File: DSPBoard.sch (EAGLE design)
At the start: 144 parts, among them IC1 AD1939WBSTZ, IC10 LM833N, IC11 LM833N, IC12 TL074P, IC2 25AA1024-I_SM, IC4 LM833N, IC5 LM833N, IC6 LM833N, IC7 LM833N, IC8 LM833N, IC9 LM833N, SW1 EC12E_SW, SW2 EC12E_SW, X1 2510-, Y1 12.288MHz

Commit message: futher effort and set 3v3 analog
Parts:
- removed C32, C33, C34, C35, C36, C37, C38, C39: 1u, rcl:C-EUC0805
- removed IC10, IC11, IC4, IC5, IC6, IC7, IC8, IC9: LM833N, linear:LM833N
- removed IC12: TL074P, linear:TL074P
- removed R30, R33, R37, R39: 200k, rcl:R-EU_R0603
- removed R31, R34, R38, R41: 33k, rcl:R-EU_R0603
- removed R32, R35, R36, R40: 100k, rcl:R-EU_R0603
- removed R42, R43, R44, R45, R46, R47, R48, R49, R50, R51: 10k, rcl:R-EU_R0603
- removed SW1, SW2: EC12E_SW, switch-alps:EC12E_SW
- removed U$13, U$14, U$15, U$16, U$17, U$18, U$19, U$20, U$21, U$22, U$23, U$24, U$5, U$6, U$7, U$9: WQP-PJ301M-12_JACK, thonkiconn:WQP-PJ301M-12_JACK
- removed VR1, VR2, VR7, VR8: 10k, SparkFun-Resistors:POTENTIOMETER-PTH-9MM-1/20W-20%-KIT
- added C45: (no value), rcl:C-EUC0805
- added IC3: LM4040B10DBZ, texas:LM4041B12DBZ
- added R16: (no value), rcl:R-EU_R0805
- added U$12, U$8: EEE-FK1C100R, LM11173p3:EEE-FK1C100R
- added U1: Value, LM11173p3:LM1117DTX-3.3/NOPB
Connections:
- removed net N$10: C32.1, IC12A.-IN, R30.2, R31.1, R32.1
- removed net N$11: R36.2, U$7.2
- removed net N$12: R30.1, VR1.S
- removed net N$13: R35.2, U$6.2
- removed net N$14: R33.2, VR2.S
- removed net N$15: C33.1, IC12B.-IN, R33.1, R34.1, R35.1
- removed net N$16: R37.2, VR7.S
- removed net N$17: C34.2, IC12C.-IN, R36.1, R37.1, R38.2
- removed net N$18: R39.2, VR8.S
- removed net N$19: R40.2, U$9.2
- removed net N$20: C35.2, IC12D.-IN, R39.1, R40.1, R41.2
- removed net N$22: R42.1, R45.1, SW1G$1.A
- removed net N$23: R43.2, R44.1, SW1G$1.B
- removed net N$25: R46.1, R49.1, SW2G$1.A
- removed net N$26: R47.2, R48.1, SW2G$1.B
- removed net N$9: R32.2, U$5.2
- removed net VSS: IC12A.+IN, IC12B.+IN, IC12C.+IN, IC12D.+IN
- new net 3V3A: U$8.+, U1.OUT
- net +3V3: no longer R44.2, R45.2, R48.2, R49.2, R50.1, R51.1
- net +5V: now also U$12.+, U1.INPUT
- net -10V: now also C45.1, IC3.A, R16.1; no longer VR1.A, VR2.A, VR7.A, VR8.A
- net -12V: now also R16.2
- net CV0: no longer C32.2, IC12A.OUT, R31.2
- net CV1: no longer C33.2, IC12B.OUT, R34.2
- net CV2: no longer C34.1, IC12C.OUT, R38.1
- net CV3: no longer C35.1, IC12D.OUT, R41.1
- net ENCODER0_0: no longer C36.1, R42.2
- net ENCODER0_1: no longer C37.1, R43.1
- net ENCODER0_2: no longer R50.2, SW1G$2.1
- net ENCODER1_0: no longer C38.1, R46.2
- net ENCODER1_1: no longer C39.1, R47.1
- net ENCODER1_2: no longer R51.2, SW2G$2.1
- net GND: now also C45.2, IC3.C, U$12.-, U$8.-, U1.GND; no longer C36.2, C37.2, C38.2, C39.2, SW1G$1.C, SW1G$2.2, SW2G$1.C, SW2G$2.2, U$5.1, U$5.3, U$6.1, U$6.3, U$7.1, U$7.3, U$9.1, U$9.3, VR1.E, VR2.E, VR7.E, VR8.E
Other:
- note added: "3v3 Analog Supply"
- note added: "3v3 Digital Supply"
- note removed: "3v2 Digital Supply"
- note removed: "Rotary Encoders"
- note removed: "This circuit is Biased by VSS at ~1v2 to give a 0 <> 3v3 signal"

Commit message: added input single to differential circuit
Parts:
- added C32: 22u, rcl:C-EUC0805
- added C33, C34, C35, C36, C37, C38, C39, C46, C47, C48, C49, C50, C51, C52, C53, C54, C55, C56, C57, C58, C59, C60, C61, C62, C63, C64, C65, C66, C67, C68, C69, C70, C71, C72, C73, C74, C75, C76, C77, C78: (no value), rcl:C-EUC0805
- added IC4, IC5, IC6, IC7: LM833D, linear:LM833D
- added R30: 480, rcl:R-EU_R0805
- added R31, R33, R34, R35, R36, R37, R38, R39, R40, R41, R42, R43, R44, R45, R46, R47, R48, R49, R50, R51, R55, R57, R61, R62, R63, R64, R65, R66, R67, R68, R69, R70, R71, R72, R73, R74, R75, R76, R77, R78: (no value), rcl:R-EU_R0805
- added R32: 10k, rcl:R-EU_R0805
- added U$21, U$5, U$6, U$7: WQP-PJ301M-12_JACK, thonkiconn:WQP-PJ301M-12_JACK
- added VR1: (no value), v-reg:TL431CLP
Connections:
- new net 1VREF: C32.1, R30.2, R32.2, VR1.C, VR1.R
- new net AIN0+: C47.1, C48.1, IC1.ADC1LP, R40.1
- new net AIN0-: C46.2, C47.2, IC1.ADC1LN, R41.1
- new net AIN1+: C57.1, C58.1, IC1.ADC1RP, R50.1
- new net AIN1-: C56.2, C57.2, IC1.ADC1RN, R51.1
- new net AIN2+: C67.1, C68.1, IC1.ADC2LP, R67.1
- new net AIN2-: C66.2, C67.2, IC1.ADC2LN, R68.1
- new net AIN3+: C76.2, C77.2, IC1.ADC2RP, R78.1
- new net AIN3-: C77.1, C78.1, IC1.ADC2RN, R77.1
- new net N$10: C35.2, R31.1
- new net N$11: C36.1, R31.2, R33.1, R39.2
- new net N$12: C37.2, IC4A.+IN, R33.2
- new net N$13: IC4B.-IN, R34.1, R35.2
- new net N$14: C36.2, IC4A.-IN, IC4A.OUT, R34.2, R41.2
- new net N$15: IC4B.OUT, R35.1, R40.2
- new net N$16: C38.2, IC4B.+IN, R36.1
- new net N$18: C38.1, C39.1, R36.2, R37.2, R38.1, R39.1
- new net N$19: C39.2, R37.1
- new net N$20: C46.1, C48.2
- new net N$23: C51.1, U$5.2
- new net N$25: C51.2, R42.1
- new net N$26: C52.1, R42.2, R43.1, R49.2
- new net N$34: C53.2, IC5A.+IN, R43.2
- new net N$36: C52.2, IC5A.-IN, IC5A.OUT, R44.2, R51.2
- new net N$38: IC5B.-IN, R44.1, R45.2
- new net N$42: IC5B.OUT, R45.1, R50.2
- new net N$43: C54.2, IC5B.+IN, R46.1
- new net N$44: C54.1, C55.1, R46.2, R47.2, R48.1, R49.1
- new net N$45: C55.2, R47.1
- new net N$46: C56.1, C58.2
- new net N$47: C61.1, U$6.2
- new net N$48: C61.2, R55.1
- new net N$49: C62.1, R55.2, R57.1, R66.2
- new net N$50: C63.2, IC6A.+IN, R57.2
- new net N$51: C62.2, IC6A.-IN, IC6A.OUT, R61.2, R68.2
- new net N$52: IC6B.-IN, R61.1, R62.2
- new net N$53: IC6B.OUT, R62.1, R67.2
- new net N$54: C64.2, IC6B.+IN, R63.1
- new net N$55: C64.1, C65.1, R63.2, R64.2, R65.1, R66.1
- new net N$56: C65.2, R64.1
- new net N$57: C66.1, C68.2
- new net N$58: C71.1, U$7.2
- new net N$59: C71.2, R69.1
- new net N$60: C72.1, R69.2, R70.1, R76.2
- new net N$61: C73.2, IC7A.+IN, R70.2
- new net N$62: C72.2, IC7A.-IN, IC7A.OUT, R71.2, R78.2
- new net N$63: IC7B.-IN, R71.1, R72.2
- new net N$64: IC7B.OUT, R72.1, R77.2
- new net N$65: C74.2, IC7B.+IN, R73.1
- new net N$66: C74.1, C75.1, R73.2, R74.2, R75.1, R76.1
- new net N$67: C75.2, R74.1
- new net N$68: C76.1, C78.2
- new net N$9: C35.1, U$21.2
- net +12V: now also C33.1, C49.1, C59.1, C69.1, IC4P.V+, IC5P.V+, IC6P.V+, IC7P.V+
- net +5V: now also R30.1
- net -12V: now also C34.2, C50.2, C60.2, C70.2, IC4P.V-, IC5P.V-, IC6P.V-, IC7P.V-
- net 3V3A: now also R38.2, R48.2, R65.2, R75.2
- net GND: now also C32.2, C33.2, C34.1, C49.2, C50.1, C59.2, C60.1, C69.2, C70.1, R32.1, VR1.A
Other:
- note added: "1v2 supply"

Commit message: added analog output circuitry
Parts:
- added C100, C102, C103, C104, C106, C107, C108, C110, C79, C80, C82, C83, C84, C86, C87, C88, C90, C91, C92, C94, C95, C96, C98, C99: 1nf, rcl:C-EUC0805
- added C101, C105, C109, C81, C85, C89, C93, C97: (no value), rcl:C-EUC0805
- added IC10, IC11, IC8, IC9: LM833D, linear:LM833D
- added R100, R107, R114, R121, R128, R79, R86, R93: 100R, rcl:R-EU_R0805
- added R101, R103, R104, R106, R108, R110, R111, R113, R115, R117, R118, R120, R122, R124, R125, R127, R129, R131, R132, R134, R80, R82, R83, R85, R87, R89, R90, R92, R94, R96, R97, R99: 2.2k, rcl:R-EU_R0805
- added R102, R105, R109, R112, R116, R119, R123, R126, R130, R133, R81, R84, R88, R91, R95, R98: 68R, rcl:R-EU_R0805
- added U$13, U$14, U$15, U$16, U$17, U$18, U$19, U$9: WQP-PJ301M-12_JACK, thonkiconn:WQP-PJ301M-12_JACK
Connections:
- new net AOUT0+: IC1.OL1P, R111.1
- new net AOUT0-: IC1.OL1N, R110.1
- new net AOUT1+: IC1.OR1P, R118.1
- new net AOUT1-: IC1.OR1N, R117.1
- new net AOUT2+: IC1.OL2P, R125.1
- new net AOUT2-: IC1.OL2N, R124.1
- new net AOUT3+: IC1.OR2P, R132.1
- new net AOUT3-: IC1.OR2N, R131.1
- new net AOUT4+: IC1.OL3P, R83.1
- new net AOUT4-: IC1.OL3N, R82.1
- new net AOUT5+: IC1.OR3P, R90.1
- new net AOUT5-: IC1.OR3N, R89.1
- new net AOUT6+: IC1.OL4P, R97.1
- new net AOUT6-: IC1.OL4N, R96.1
- new net AOUT7+: IC1.OR4P, R104.1
- new net AOUT7-: IC1.OR4N, R103.1
- new net N$100: C100.1, IC10B.OUT, R114.1, R115.2
- new net N$101: C100.2, IC10B.-IN, R116.2
- new net N$102: C101.1, R115.1, R116.1, R117.2
- new net N$103: C101.2, R118.2, R119.1, R120.2
- new net N$104: C102.1, IC10B.+IN, R119.2
- new net N$105: C103.2, R121.2, U$18.2
- new net N$106: C104.1, IC11A.OUT, R121.1, R122.2
- new net N$107: C104.2, IC11A.-IN, R123.2
- new net N$108: C105.1, R122.1, R123.1, R124.2
- new net N$109: C105.2, R125.2, R126.1, R127.2
- new net N$110: C106.1, IC11A.+IN, R126.2
- new net N$111: C107.2, R128.2, U$19.2
- new net N$112: C108.1, IC11B.OUT, R128.1, R129.2
- new net N$113: C108.2, IC11B.-IN, R130.2
- new net N$114: C109.1, R129.1, R130.1, R131.2
- new net N$115: C109.2, R132.2, R133.1, R134.2
- new net N$116: C110.1, IC11B.+IN, R133.2
- new net N$17: C79.2, R79.2, U$9.2
- new net N$22: C80.1, IC8A.OUT, R79.1, R80.2
- new net N$69: C81.2, R83.2, R84.1, R85.2
- new net N$70: C80.2, IC8A.-IN, R81.2
- new net N$71: C81.1, R80.1, R81.1, R82.2
- new net N$72: C82.1, IC8A.+IN, R84.2
- new net N$73: C83.2, R86.2, U$13.2
- new net N$74: C84.1, IC8B.OUT, R86.1, R87.2
- new net N$77: C84.2, IC8B.-IN, R88.2
- new net N$78: C85.1, R87.1, R88.1, R89.2
- new net N$79: C85.2, R90.2, R91.1, R92.2
- new net N$80: C86.1, IC8B.+IN, R91.2
- new net N$81: C87.2, R93.2, U$14.2
- new net N$82: C88.1, IC9A.OUT, R93.1, R94.2
- new net N$83: C88.2, IC9A.-IN, R95.2
- new net N$84: C89.1, R94.1, R95.1, R96.2
- new net N$85: C89.2, R97.2, R98.1, R99.2
- new net N$86: C90.1, IC9A.+IN, R98.2
- new net N$87: C91.2, R100.2, U$15.2
- new net N$88: C92.1, IC9B.OUT, R100.1, R101.2
- new net N$89: C92.2, IC9B.-IN, R102.2
- new net N$90: C93.1, R101.1, R102.1, R103.2
- new net N$91: C93.2, R104.2, R105.1, R106.2
- new net N$92: C94.1, IC9B.+IN, R105.2
- new net N$93: C95.2, R107.2, U$16.2
- new net N$94: C96.1, IC10A.OUT, R107.1, R108.2
- new net N$95: C96.2, IC10A.-IN, R109.2
- new net N$96: C97.1, R108.1, R109.1, R110.2
- new net N$97: C97.2, R111.2, R112.1, R113.2
- new net N$98: C98.1, IC10A.+IN, R112.2
- new net N$99: C99.2, R114.2, U$17.2
- net +12V: now also IC10P.V+, IC11P.V+, IC8P.V+, IC9P.V+
- net -12V: now also IC10P.V-, IC11P.V-, IC8P.V-, IC9P.V-
- net GND: now also C102.2, C103.1, C106.2, C107.1, C110.2, C79.1, C82.2, C83.1, C86.2, C87.1, C90.2, C91.1, C94.2, C95.1, C98.2, C99.1, R106.1, R113.1, R120.1, R127.1, R134.1, R85.1, R92.1, R99.1, U$13.1, U$14.1, U$15.1, U$16.1, U$17.1, U$18.1, U$19.1, U$9.1

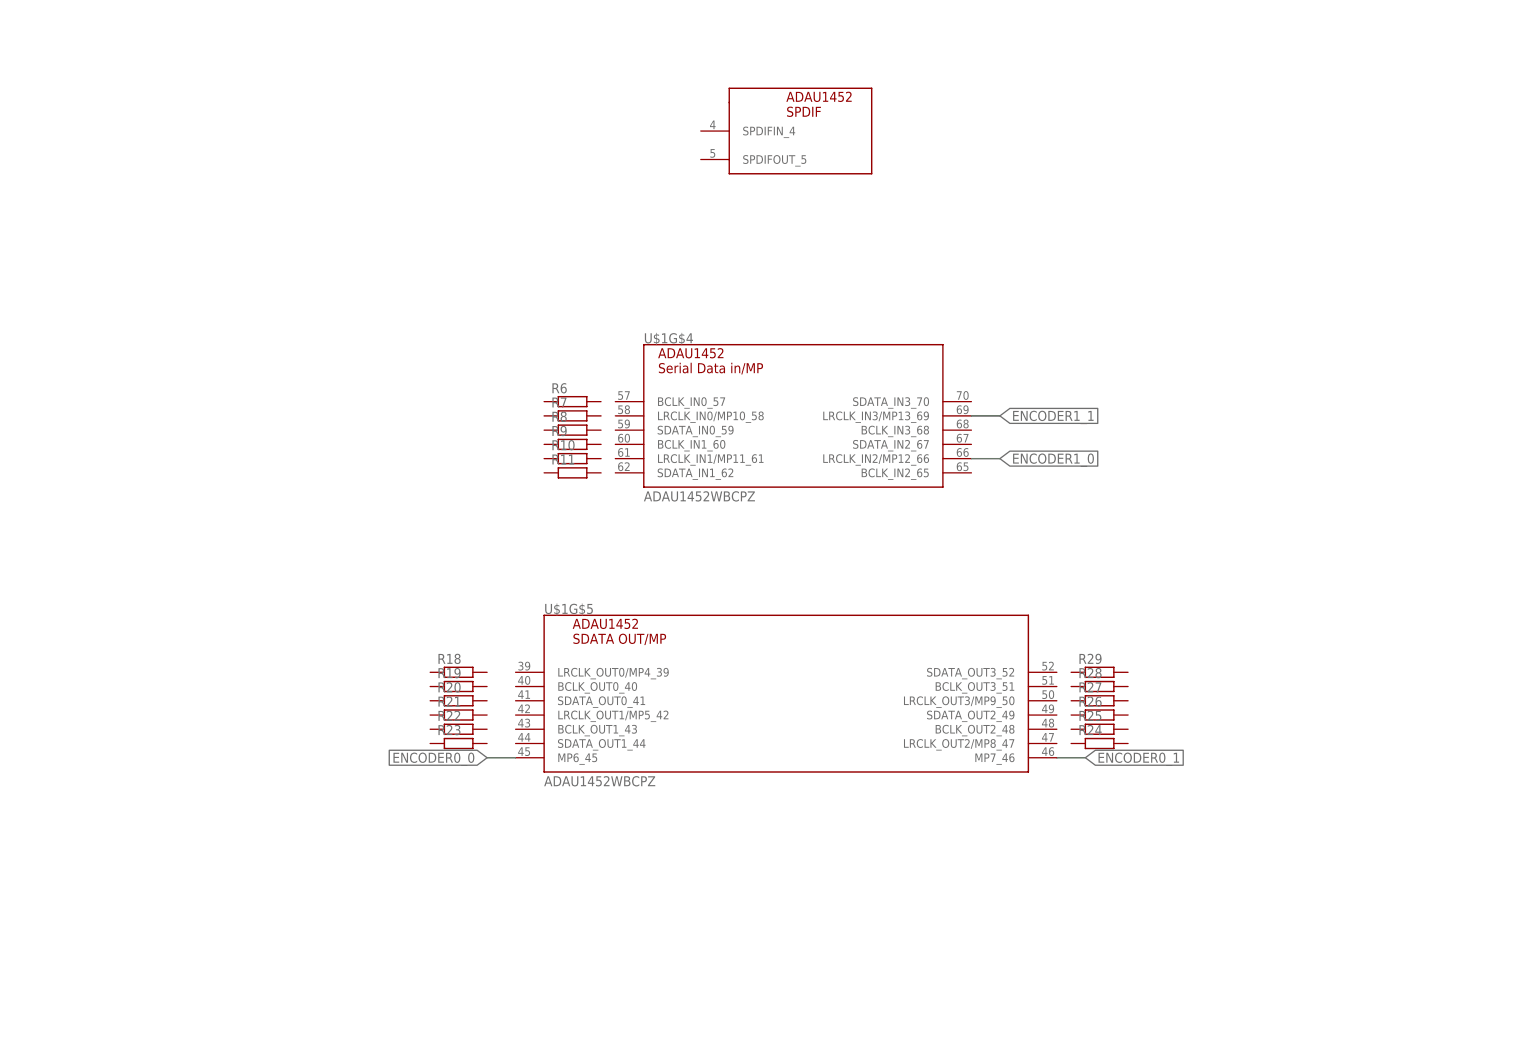
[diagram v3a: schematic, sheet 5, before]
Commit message: finished addign audio parts (still need to set values and check everyhting
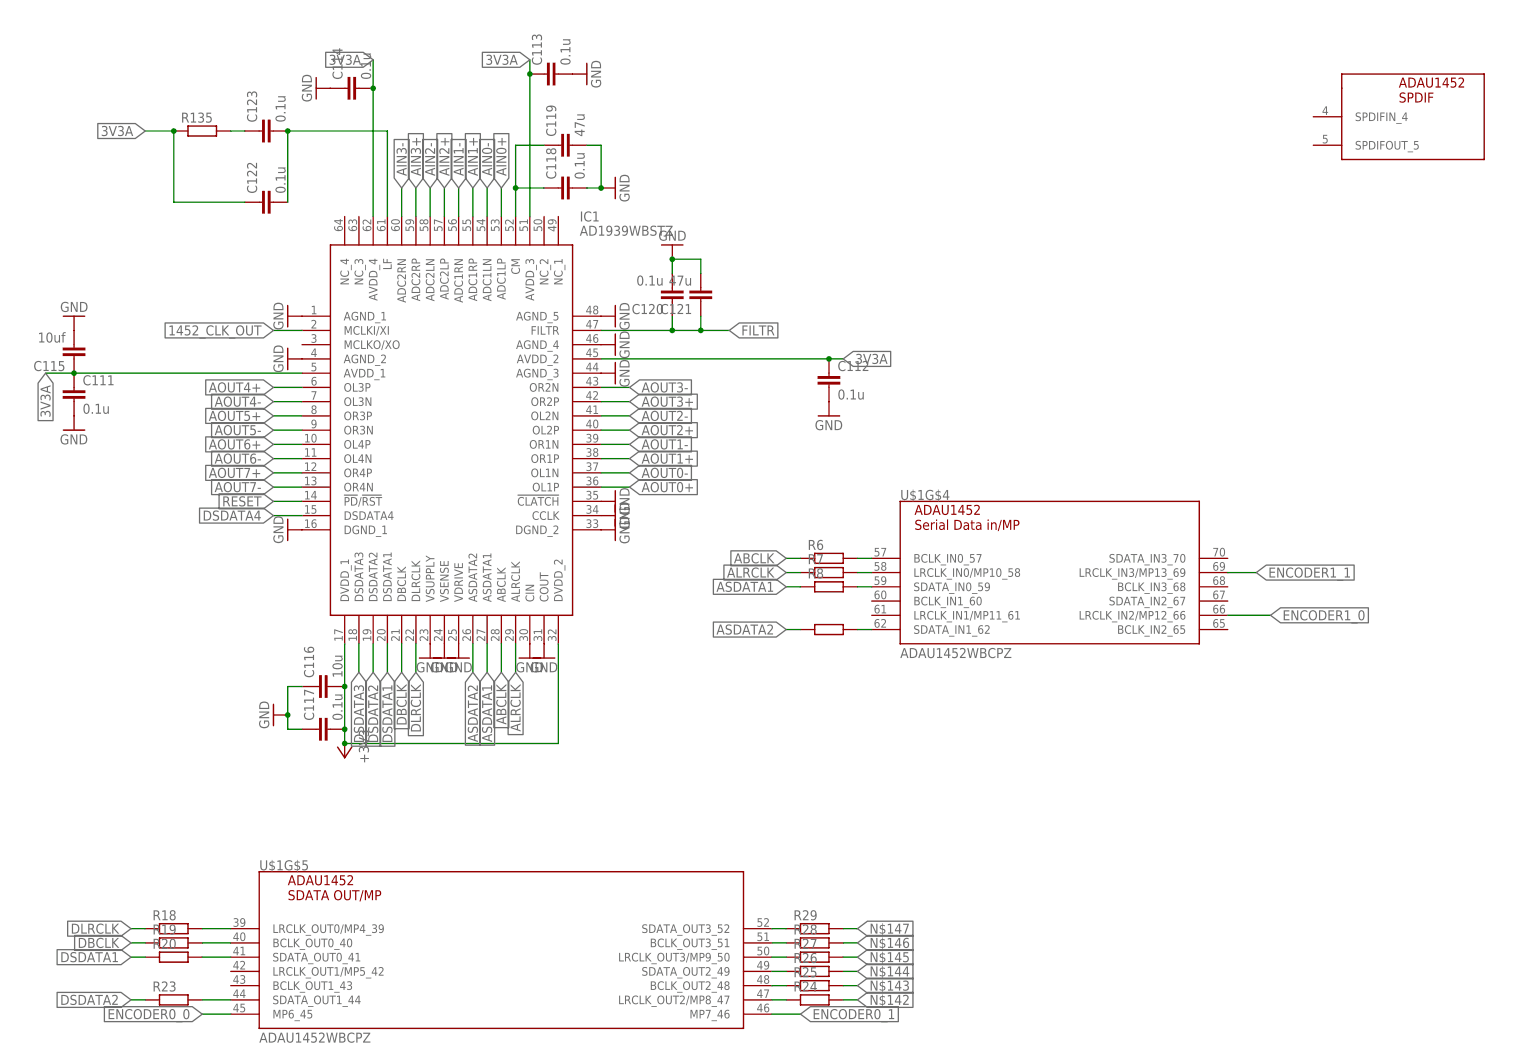
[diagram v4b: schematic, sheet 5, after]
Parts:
- removed R10, R21, R22: (no value), rcl:R-EU_R0603
- removed R84: 68R, rcl:R-EU_R0805
- added C111, C112, C113, C114, C117, C118, C120, C122, C123: 0.1u, rcl:C-EUC0805
- added C115: 10uf, rcl:C-EUC0805
- added C116: 10u, rcl:C-EUC0805
- added C119, C121: 47u, rcl:C-EUC0805
- added R135: (no value), rcl:R-EU_R0603
- R9: value (none) -> 68R; device rcl:R-EU_R0603 -> rcl:R-EU_R0805
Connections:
- removed net N$69: C81.2, R83.2, R84.1, R85.2
- new net ABCLK: IC1.ABCLK, R6.1
- new net ALRCLK: IC1.ALRCLK, R7.1
- new net ASDATA1: IC1.ASDATA1, R8.1
- new net ASDATA2: IC1.ASDATA2, R11.1
- new net DBCLK: IC1.DBCLK, R19.1
- new net DLRCLK: IC1.DLRCLK, R18.1
- new net DSDATA1: IC1.DSDATA1, R20.1
- new net DSDATA2: IC1.DSDATA2, R23.1
- new net DSDATA3: IC1.DSDATA3
- new net DSDATA4: IC1.DSDATA4
- new net FILTR: C120.1, C121.1, IC1.FILTR
- new net N$117: C123.1, R135.2
- new net N$118: R7.2, U$1G$4.LRCLK_IN0/MP10_58
- new net N$119: C122.2, C123.2, IC1.LF
- new net N$120: R8.2, U$1G$4.SDATA_IN0_59
- new net N$121: C81.2, R83.2, R85.2, R9.1
- new net N$123: R11.2, U$1G$4.SDATA_IN1_62
- new net N$124: R23.2, U$1G$5.SDATA_OUT1_44
- new net N$127: R20.2, U$1G$5.SDATA_OUT0_41
- new net N$128: R19.2, U$1G$5.BCLK_OUT0_40
- new net N$129: R18.2, U$1G$5.LRCLK_OUT0/MP4_39
- new net N$136: R29.1, U$1G$5.SDATA_OUT3_52
- new net N$137: R28.1, U$1G$5.BCLK_OUT3_51
- new net N$138: R27.1, U$1G$5.LRCLK_OUT3/MP9_50
- new net N$139: R26.1, U$1G$5.SDATA_OUT2_49
- new net N$140: R25.1, U$1G$5.BCLK_OUT2_48
- new net N$141: R24.1, U$1G$5.LRCLK_OUT2/MP8_47
- new net N$142: R24.2
- new net N$143: R25.2
- new net N$144: R26.2
- new net N$145: R27.2
- new net N$146: R28.2
- new net N$147: R29.2
- new net N$75: C118.1, C119.1, IC1.CM
- new net N$76: R6.2, U$1G$4.BCLK_IN0_57
- net +3V3: now also C116.2, C117.2, IC1.DVDD_1, IC1.DVDD_2
- net 1452_CLK_OUT: now also IC1.MCLKI/XI
- net 3V3A: now also C111.1, C112.1, C113.1, C114.2, C115.1, C122.1, IC1.AVDD_1, IC1.AVDD_2, IC1.AVDD_3, IC1.AVDD_4, R135.1
- net GND: now also C111.2, C112.2, C113.2, C114.1, C115.2, C116.1, C117.1, C118.2, C119.2, C120.2, C121.2, IC1.!CLATCH, IC1.AGND_1, IC1.AGND_2, IC1.AGND_3, IC1.AGND_4, IC1.AGND_5, IC1.CCLK, IC1.CIN, IC1.COUT, IC1.DGND_1, IC1.DGND_2, IC1.VDRIVE, IC1.VSENSE, IC1.VSUPPLY
- net N$72: now also R9.2; no longer R84.2
- net RESET: now also IC1.!PD!/!RST
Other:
- moved on the sheet: R18, R19, R20, R23, R24, R25, R26, R27, R28, R29, R6, R7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

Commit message: encoders and CV parts placed in sch
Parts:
- added C124, C125, C126, C127: (no value), rcl:C-EUC0805
- added C128, C129, C130, C131: 0.1u, rcl:C-EUC0805
- added IC12: TL074D, linear:TL074D
- added R10, R140, R141, R21, R22, R84: 10k, rcl:R-EU_R0805
- added R136, R137, R138: (no value), rcl:R-EU_R0805
- added R139, R145, R148, R151: 100k, rcl:R-EU_R0805
- added R142: (no value), rcl:R-EU_R0603
- added R143, R146, R149, R152: 33k, rcl:R-EU_R0805
- added R144, R147, R150, R153: 200k, rcl:R-EU_R0805
- added U$20, U$22, U$23, U$24: WQP-PJ301M-12_JACK, thonkiconn:WQP-PJ301M-12_JACK
- added U2, U3: PEC11R-4315F-N0012, SamacSys_Parts:PEC11R-4315F-N0012
- added VR2, VR3, VR4, VR5: 10k, SparkFun-Resistors:POTENTIOMETER-PTH-9MM-1/20W-20%-KIT
- R28: device rcl:R-EU_R0603 -> rcl:R-EU_R0805
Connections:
- new net N$122: R139.1, U$20.2
- new net N$125: R137.2, R22.1, U3.A
- new net N$126: R144.1, VR2.S
- new net N$130: R142.2, U$1G$5.LRCLK_OUT1/MP5_42
- new net N$131: R138.2, R84.2, U3.C
- new net N$132: C128.1, IC12A.-IN, R139.2, R143.2, R144.2
- new net N$133: R136.2, R21.2, U2.C
- new net N$134: R145.1, U$22.2
- new net N$135: R147.1, VR3.S
- new net N$148: C130.1, IC12C.-IN, R148.2, R149.2, R150.2
- new net N$149: R151.1, U$24.2
- new net N$150: R153.1, VR5.S
- new net N$151: C131.1, IC12D.-IN, R151.2, R152.2, R153.2
- new net N$69: R10.1, R28.2, U2.A
- new net SW0: R140.2, R142.1, U2.COM
- new net SW1: R141.2, R27.2, U3.COM
- net +12V: now also IC12P.V+
- net +3V3: now also R136.1, R137.1, R138.1, R140.1, R141.1, R28.1
- net -10V: now also VR2.E, VR3.E, VR4.E, VR5.E
- net -12V: now also IC12P.V-
- net 1VREF: now also IC12A.+IN, IC12B.+IN, IC12C.+IN, IC12D.+IN
- net CV0: now also C128.2, IC12A.OUT, R143.1
- net CV1: now also C129.2, IC12B.OUT, R146.1
- net CV2: now also C130.2, IC12C.OUT, R149.1
- net CV3: now also C131.2, IC12D.OUT, R152.1
- net ENCODER0_0: now also C125.1, R10.2
- net ENCODER0_1: now also C124.1, R21.1
- net ENCODER1_0: now also C126.1, R22.2
- net ENCODER1_1: now also C127.1, R84.1
- net GND: now also C124.2, C125.2, C126.2, C127.2, C37.1, C53.1, C63.1, C73.1, U$20.1, U$20.3, U$22.1, U$22.3, U$23.1, U$23.3, U$24.1, U$24.3, U2.B, U2.NO, U3.B, U3.NO, VR2.A, VR3.A, VR4.A, VR5.A
- net N$137: now also C129.1, IC12B.-IN, R145.2, R146.2, R147.2; no longer R28.1, U$1G$5.BCLK_OUT3_51
- net N$145: now also R148.1, U$23.2; no longer R27.2
- net N$146: now also R150.1, VR4.S; no longer R28.2
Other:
- note removed: "VEE is 1v2 for the DSP"
- note removed: "VSS is also 1.2, but for an analog use as opposed to digital"
